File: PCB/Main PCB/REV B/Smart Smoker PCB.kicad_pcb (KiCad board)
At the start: 4 copper layers, 90 x 45 mm, 80 parts, among them J1 105017-0001, J2 393570002, J3 393570002, J4 393570002, J5 393570002, J6 393570002, J7 393570002, J8 Hopper, J9 Lid, Q1 Q_PMOS_GSD, Q2 25V 1.5A Trans, Q3 25V 1.5A Trans, Q4 Q_PMOS_GSD, Q5 2N7002T-7-F, Q6 2N7002T-7-F, U1 ESP32-WROOM-32UE_16MB, U2 DG409LEDY-T1-GE3, U3 MAX31855KASA, U4 AMS1117-3.3, U5 CP2102N-Axx-xQFN28, U6 LTC4412xS6

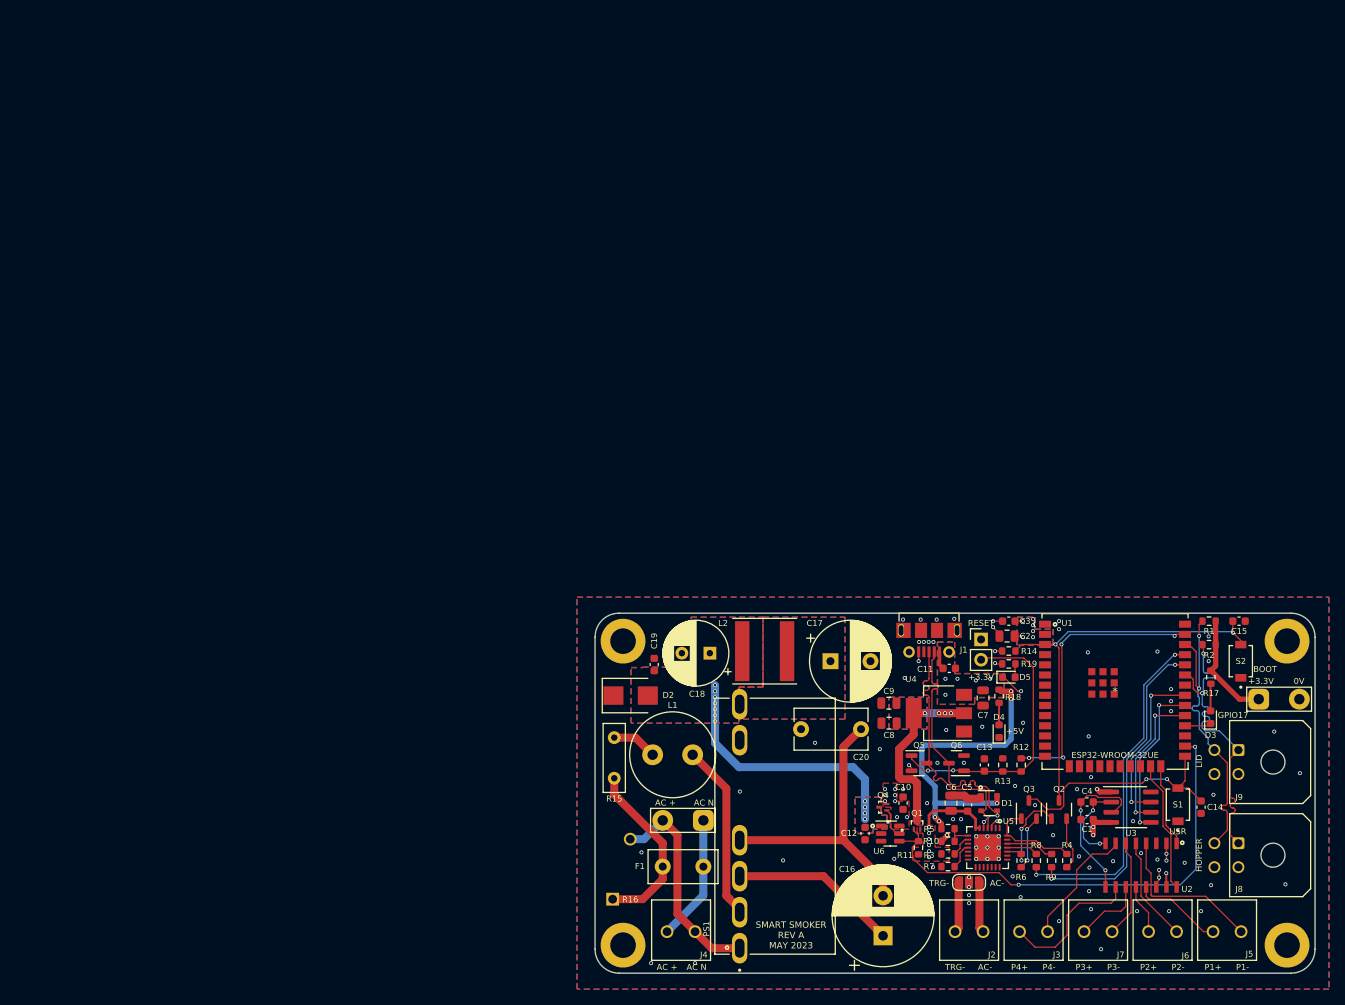
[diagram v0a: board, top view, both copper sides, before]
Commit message: Hardware Rev B development Relays and Rotary Encoder
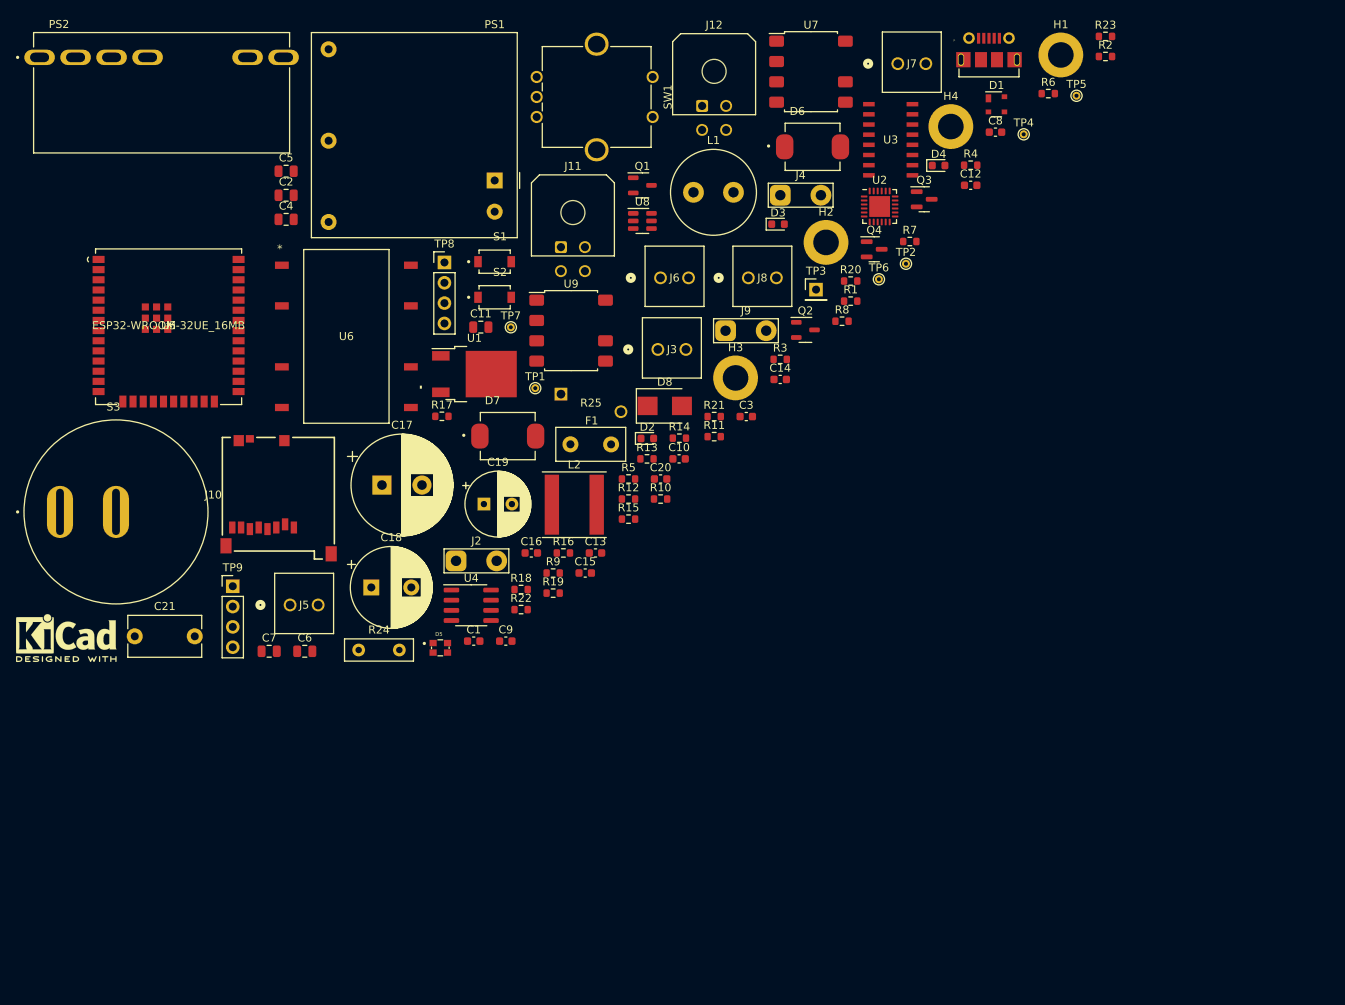
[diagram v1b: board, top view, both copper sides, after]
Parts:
- removed JP1: Jumper_2_Open, Connector_PinHeader_2.54mm:PinHeader_1x02_P2.54mm_Vertical
- removed JP2: Jumper_3_Open, Jumper:SolderJumper-3_P1.3mm_Open_RoundedPad1.0x1.5mm
- removed Q5, Q6: 2N7002T-7-F, Package_TO_SOT_SMD:SOT-23
- added C21: 1000pF 440VAC Y5P, Capacitor_THT:C_Disc_D9.0mm_W5.0mm_P7.50mm, F.Cu at (42.5, 102.9)
- added D6: D_TVS, Customs Smoker:DIOM7959X262N, F.Cu at (127.2, 41.7)
- added D7: D_TVS, Customs Smoker:DIOM7959X262N, F.Cu at (89.1, 77.9)
- added D8: TVS DIODE 7VWM 12VC SMB, Diode_SMD:D_SMB, F.Cu at (108.7, 74.1)
- added J10: MEM2051-00-195-00-A, Customs Smoker:GCT_MEM2051-00-195-00-A, F.Cu at (60.4, 85.6)
- added J11: Hopper, Connector_Molex:Molex_Micro-Fit_3.0_43045-0400_2x02_P3.00mm_Horizontal, F.Cu at (95.7, 54.2)
- added J12: Lid, Connector_Molex:Molex_Micro-Fit_3.0_43045-0400_2x02_P3.00mm_Horizontal, F.Cu at (113.4, 36.6)
- added PS2: LS10-13B03R3, Customs Smoker:CONV_LS10-13B03R3, F.Cu at (45.8, 30.5)
- added R20: 80.6Ohm 1% 0603, Resistor_SMD:R_0603_1608Metric, F.Cu at (132.0, 58.5)
- added R21: 470Ohm 5% 0603, Resistor_SMD:R_0603_1608Metric, F.Cu at (114.9, 75.4)
- added R22: 140Ohm 1% 0603, Resistor_SMD:R_0603_1608Metric, F.Cu at (90.8, 99.6)
- added R23: 80.6Ohm 1% 0603, Resistor_SMD:R_0603_1608Metric, F.Cu at (163.8, 27.9)
- added R24: 6.8Ohm 3W 5% 2512, Resistor_THT:R_Box_L8.4mm_W2.5mm_P5.08mm, F.Cu at (70.5, 104.6)
- added R25: B72214S0351K101, Customs Smoker:VARS_B72214S_15P5X5P6-7P5-2P2_TDK, F.Cu at (99.5, 73.7)
- added S3: RR511D1121, Customs Smoker:E-SWITCH_RR511D1121, F.Cu at (40.1, 87.3)
- added SW1: SW_Coded_SH-7050, Rotary_Encoder:RotaryEncoder_Bourns_Vertical_PEC12R-3xxxF-Sxxxx, F.Cu at (92.7, 33.0)
- added TP3: GND TP PIN, Connector_PinHeader_2.54mm:PinHeader_1x01_P2.54mm_Vertical, F.Cu at (127.6, 59.6)
- added TP4: 3V3 TP, TestPoint:TestPoint_THTPad_D1.0mm_Drill0.5mm, F.Cu at (153.6, 40.1)
- added TP5: 3V3 TP, TestPoint:TestPoint_THTPad_D1.0mm_Drill0.5mm, F.Cu at (160.2, 35.3)
- added TP6: SCL TP, TestPoint:TestPoint_THTPad_D1.0mm_Drill0.5mm, F.Cu at (135.5, 58.3)
- added TP7: SDA TP, TestPoint:TestPoint_THTPad_D1.0mm_Drill0.5mm, F.Cu at (89.5, 64.3)
- added TP8: GPIO MISC., Connector_PinHeader_2.54mm:PinHeader_1x04_P2.54mm_Vertical, F.Cu at (81.2, 56.2)
- added TP9: Screen I2C, Connector_PinHeader_2.54mm:PinHeader_1x04_P2.54mm_Vertical, F.Cu at (54.7, 96.6)
- added U7: AQH2223A, Package_SO:SSO-7-8_6.4x9.78mm_P2.54mm, F.Cu at (127.0, 32.3)
- added U8: LTC4412xS6, Package_TO_SOT_SMD:TSOT-23-6, F.Cu at (105.9, 51.0)
- added U9: AQH2223A, Package_SO:SSO-7-8_6.4x9.78mm_P2.54mm, F.Cu at (97.0, 64.7)
- AE1: moved to F.Cu
- C10: value 1uF 25V X5R 0603 -> 0.01uF 50V X7R 0603
- C11: value 0.1uF 50V X7R 0603 -> 22uF 10V X5R 0805; footprint Capacitor_SMD:C_0603_1608Metric -> Capacitor_SMD:C_0805_2012Metric
- C15: value 0.1uF 50V X7R 0603 -> 1uF 25V X5R 0603
- C16: value 22uF 450V 20% -> 0.1uF 50V X7R 0603; footprint Capacitor_THT:CP_Radial_D12.5mm_P5.00mm -> Capacitor_SMD:C_0603_1608Metric
- C17: value 820uF 20% 16V -> 22uF 450V 20%; footprint Capacitor_THT:CP_Radial_D10.0mm_P5.00mm -> Capacitor_THT:CP_Radial_D12.5mm_P5.00mm
- C18: value 150uF 20% 35V -> 820uF 20% 16V; footprint Capacitor_THT:CP_Radial_D8.0mm_P3.50mm -> Capacitor_THT:CP_Radial_D10.0mm_P5.00mm
- C19: value 0.1uF 50V X7R 0603 -> 150uF 20% 35V; footprint Capacitor_SMD:C_0603_1608Metric -> Capacitor_THT:CP_Radial_D8.0mm_P3.50mm
- C2: value 22uF 10V X5R 0805 -> 4.7uF 25V X5R 0805
- C20: value 1000pF 440VAC Y5P -> 0.1uF 50V X7R 0603; footprint Capacitor_THT:C_Disc_D9.0mm_W5.0mm_P7.50mm -> Capacitor_SMD:C_0603_1608Metric
- C4: value 0.01uF 50V X7R 0603 -> 10uF 16V X5R 0805; footprint Capacitor_SMD:C_0603_1608Metric -> Capacitor_SMD:C_0805_2012Metric
- C5: value 0.1uF 50V X7R 0603 -> 10uF 16V X5R 0805; footprint Capacitor_SMD:C_0603_1608Metric -> Capacitor_SMD:C_0805_2012Metric
- C6: value 4.7uF 25V X5R 0805 -> 10uF 16V X5R 0805
- C8, C9: value 10uF 16V X5R 0805 -> 0.1uF 50V X7R 0603; footprint Capacitor_SMD:C_0805_2012Metric -> Capacitor_SMD:C_0603_1608Metric
- D2: value TVS DIODE 7VWM 12VC SMB -> Y 2V 20mA; footprint Diode_SMD:D_SMB -> LED_SMD:LED_0603_1608Metric
- D3: value Y 2V 20mA -> Y/G 2.2V 20mA
- D4: value Y/G 2.2V 20mA -> R 1.8V 2mA 0603
- D5: value R 1.8V 2mA 0603 -> ASMB-KTF0-0A306; footprint LED_SMD:LED_0603_1608Metric -> Customs Smoker:LED_ASMB-KTF0-0A306
- J2: value 393570002 -> HEATER; footprint Customs Smoker:CONN_393570002_MOL -> TestPoint:TestPoint_2Pads_Pitch5.08mm_Drill1.3mm
- J4: value 393570002 -> AUGER; footprint Customs Smoker:CONN_393570002_MOL -> TestPoint:TestPoint_2Pads_Pitch5.08mm_Drill1.3mm
- J8: value Hopper -> 393570002; footprint Connector_Molex:Molex_Micro-Fit_3.0_43045-0400_2x02_P3.00mm_Horizontal -> Customs Smoker:CONN_393570002_MOL
- J9: value Lid -> FAN; footprint Connector_Molex:Molex_Micro-Fit_3.0_43045-0400_2x02_P3.00mm_Horizontal -> TestPoint:TestPoint_2Pads_Pitch5.08mm_Drill1.3mm
- PS1: value LS10-13B03R3 -> RAC05-3.3SK; footprint Customs Smoker:CONV_LS10-13B03R3 -> Converter_ACDC:Converter_ACDC_RECOM_RAC05-xxSK_THT
- Q1: value Q_PMOS_GSD -> 25V 1.5A Trans; footprint Customs Smoker:VESM_TOS -> Package_TO_SOT_SMD:SOT-23-3
- Q3: value 25V 1.5A Trans -> Q_PMOS_GSD; footprint Package_TO_SOT_SMD:SOT-23-3 -> Package_TO_SOT_SMD:SOT-23
- Q4: footprint Customs Smoker:VESM_TOS -> Package_TO_SOT_SMD:SOT-23
- R1: value 1.8kOhm 1% 0603 -> 1kOhm 1% 0603
- R10: value 47.5kOhm 1% 0603 -> 10K 1% 0603
- R11: value 470Ohm 5% 0603 -> 470Ohm 1% 0603
- R12: value 1kOhm 1% 0603 -> 140Ohm 1% 0603
- R13: value 10K 1% 0603 -> 140Ohm 1% 0603
- R14: value 10K 1% 0603 -> 750Ohm 1% 0603
- R15: value 6.8Ohm 3W 5% 2512 -> 80.6Ohm 1% 0603; footprint Resistor_THT:R_Box_L8.4mm_W2.5mm_P5.08mm -> Resistor_SMD:R_0603_1608Metric
- R16: value B72214S0351K101 -> 20Ohm 1% 0603; footprint Customs Smoker:VARS_B72214S_15P5X5P6-7P5-2P2_TDK -> Resistor_SMD:R_0603_1608Metric
- R17: value 470Ohm 1% 0603 -> 20Ohm 1% 0603
- R18: value 140Ohm 1% 0603 -> 64.9Ohm 1% 0603
- R19: value 750Ohm 1% 0603 -> 140Ohm 1% 0603
- R2: value 1.8kOhm 1% 0603 -> 10K 1% 0603
- R3: value 1kOhm 1% 0603 -> 22.1kOhm 1% 0603
- R5: value 22.1kOhm 1% 0603 -> 47.5kOhm 1% 0603
- R6, R7: value 10K 1% 0603 -> 0Ohm 0603
- R8, R9: value 0Ohm 0603 -> 1.8kOhm 1% 0603
- TP1: value TestPoint_2Pole -> 3V3 TP; footprint TestPoint:TestPoint_2Pads_Pitch5.08mm_Drill1.3mm -> TestPoint:TestPoint_THTPad_D1.0mm_Drill0.5mm
- TP2: value TestPoint_2Pole -> GND TP; footprint TestPoint:TestPoint_2Pads_Pitch5.08mm_Drill1.3mm -> TestPoint:TestPoint_THTPad_D1.0mm_Drill0.5mm
- U1: value ESP32-WROOM-32UE_16MB -> AMS1117-3.3; footprint Customs Smoker:ESP32-WROOM-32UE 16MB -> Package_TO_SOT_SMD:TO-252-2
- U2: value DG409LEDY-T1-GE3 -> CP2102N-Axx-xQFN20; footprint Customs Smoker:SOIC16_NARROW_VIS -> Package_DFN_QFN:QFN-24-1EP_4x4mm_P0.5mm_EP2.6x2.6mm
- U3: value MAX31855KASA -> DG409LEDY-T1-GE3; footprint Package_SO:SOIC-8_3.9x4.9mm_P1.27mm -> Customs Smoker:SOIC16_NARROW_VIS
- U4: value AMS1117-3.3 -> MAX31855KASA; footprint Package_TO_SOT_SMD:SOT-223-3_TabPin2 -> Package_SO:SOIC-8_3.9x4.9mm_P1.27mm
- U5: value CP2102N-Axx-xQFN28 -> ESP32-WROOM-32UE_16MB; footprint Package_DFN_QFN:QFN-28-1EP_5x5mm_P0.5mm_EP3.35x3.35mm -> Customs Smoker:ESP32-WROOM-32UE 16MB
- U6: value LTC4412xS6 -> CPC1966B; footprint Package_TO_SOT_SMD:TSOT-23-6 -> Customs Smoker:CPC1966B_IXY
- moved C4 123.8 mm to (61.4, 50.8)
- moved J5 122.4 mm to (61.9, 99.0)
- moved U5 121.3 mm to (46.7, 64.2), turned to 0 degrees
- moved C5 116.3 mm to (61.4, 44.8), turned to 0 degrees
- moved J7 111.0 mm to (137.8, 31.3)
- moved H4 110.2 mm to (144.5, 39.2)
- moved S1 109.1 mm to (87.4, 56.1), turned to 0 degrees
- moved C2 105.6 mm to (61.4, 47.8)
- moved H2 105.1 mm to (128.9, 53.7)
- moved S2 103.8 mm to (87.4, 60.5), turned to 0 degrees
- moved J6 102.0 mm to (108.2, 58.1)
- moved R17 101.5 mm to (80.9, 75.4), turned to 0 degrees
- moved R6 95.9 mm to (156.7, 35.1), turned to 0 degrees
- moved J8 93.5 mm to (119.2, 58.1), turned to 0 degrees
- moved J4 93.1 mm to (123.2, 47.8)
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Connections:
- C1 pad 1: +3.3V -> GND
- C1 pad 2: GND -> +3.3V
- C10 pad 1: GND -> /MUX_OUT_+
- C10 pad 2: +3.3V -> /MUX_OUT_-
- C11 pad 1: +5V -> GND
- C11 pad 2: GND -> +3.3V
- C12 pad 1: +3.3VA -> GND
- C12 pad 2: GND -> +3.3V
- C13 pad 1: GND -> /EN
- C13 pad 2: Net-(C13-Pad2) -> GND
- C14 pad 1: GND -> /IO0
- C14 pad 2: /IO0 -> GND
- C15 pad 1: /EN -> GND
- C15 pad 2: GND -> +3.3V
- C16 pad 1: Net-(C16-Pad1) -> +3.3VA
- C16 pad 2: Net-(C16-Pad2) -> GND
- C17 pad 2: GND -> Net-(C17-Pad2)
- C18 pad 1: +3.3VA -> Net-(C18-Pad1)
- C20 pad 1: Net-(C16-Pad2) -> +3.3VA
- C3 pad 1: GND -> Net-(C3-Pad1)
- C3 pad 2: +3.3V -> Net-(C3-Pad2)
- C4 pad 1: /MUX_OUT_+ -> Net-(C3-Pad2)
- C4 pad 2: /MUX_OUT_- -> Net-(C3-Pad1)
- C5 pad 1: GND -> +5V
- C5 pad 2: +3.3V -> GND
- C6 pad 1: GND -> +3.3VP
- C6 pad 2: +3.3V -> GND
- C7 pad 1: +5V -> +3.3VP
- C8 pad 1: +3.3VP -> +3.3V
- C9 pad 1: +3.3VP -> +5V
- D2 pad 1: GND -> /IO17
- D2 pad 2: +3.3VA -> Net-(D2-Pad2)
- D3 pad 1: /IO17 -> GND
- D5 pad 1: GND -> +3.3V
- J2 pad 1: /TRG_GND -> /Heater_+
- J2 pad 2: /AC_G -> /AC_N
- J4 pad 1: /AC_L -> /Auger_+
- J5 pad 1: /Probe1+ -> /AC_L
- J5 pad 2: /Probe1- -> /AC_N
- J6 pad 1: /Probe2+ -> /Probe1+
- J6 pad 2: /Probe2- -> /Probe1-
- J7 pad 1: /Probe3+ -> /Probe2+
- J7 pad 2: /Probe3- -> /Probe2-
- J8 pad 1: /I2C_SDA -> /Probe3+
- J8 pad 2: GND -> /Probe3-
- J9 pad 1: /I2C_SDA -> /Fan_+
- J9 pad 2: GND -> /AC_N
- L2 pad 1: Net-(C17-Pad1) -> Net-(C18-Pad1)
- PS1 pad 1: /AC_N -> unconnected-(PS1-Pad1)
- PS1 pad 2: Net-(L1-Pad2) -> unconnected-(PS1-Pad2)
- PS1 pad 3: Net-(C16-Pad1) -> unconnected-(PS1-Pad3)
- PS1 pad 4: Net-(C16-Pad2) -> Net-(C3-Pad1)
- PS1 pad 5: GND -> Net-(C3-Pad2)
- Q1 pad 1: /IO4 -> /RTS
- Q1 pad 2: +3.3V -> Net-(Q1-Pad2)
- Q1 pad 3: +3.3VP -> /EN
- Q2 pad 1: /RTS -> /DTR
- Q2 pad 3: /EN -> /IO0
- Q3 pad 1: /DTR -> /IO4
- Q3 pad 2: Net-(Q3-Pad2) -> +3.3V
- Q3 pad 3: /IO0 -> +3.3VP
- Q4 pad 1: Net-(Q4-Pad1) -> Net-(U8-Pad5)
- R1 pad 1: /I2C_SCL -> Net-(R1-Pad1)
- R10 pad 1: GND -> /EN
- R10 pad 2: Net-(R10-Pad2) -> +3.3V
- R11 pad 1: /IO4 -> +3.3V
- R11 pad 2: +3.3V -> Net-(D2-Pad2)
- R12 pad 1: /IO23 -> +5V
- R12 pad 2: Net-(C13-Pad2) -> Net-(D3-Pad2)
- R13 pad 1: Net-(C13-Pad2) -> unconnected-(R13-Pad1)
- R13 pad 2: GND -> Net-(R13-Pad2)
- R14 pad 1: /EN -> +3.3V
- R14 pad 2: +3.3V -> Net-(D4-Pad2)
- R15 pad 1: Net-(F1-Pad2) -> Net-(R13-Pad2)
- R15 pad 2: Net-(L1-Pad1) -> GND
- R16 pad 1: Net-(F1-Pad2) -> Net-(D5-Pad3)
- R16 pad 2: /AC_N -> /IO26
- R17 pad 1: +3.3V -> Net-(D5-Pad4)
- R17 pad 2: Net-(D3-Pad2) -> /IO27
- R18 pad 1: +5V -> Net-(D5-Pad2)
- R18 pad 2: Net-(D4-Pad2) -> /IO25
- R19 pad 1: +3.3V -> unconnected-(R19-Pad1)
- R19 pad 2: Net-(D5-Pad2) -> Net-(R19-Pad2)
- R2 pad 1: /I2C_SDA -> /DTR
- R2 pad 2: +3.3V -> Net-(Q1-Pad2)
- R3 pad 1: Net-(R3-Pad1) -> +5V
- R3 pad 2: +3.3V -> Net-(R3-Pad2)
- R4 pad 1: /DTR -> /RTS
- R5 pad 1: +5V -> GND
- R5 pad 2: Net-(R10-Pad2) -> Net-(R3-Pad2)
- R6 pad 1: /RTS -> /TXD0
- R6 pad 2: Net-(Q3-Pad2) -> /RXD
- R7 pad 1: GND -> /RXD0
- R7 pad 2: Net-(R7-Pad2) -> /TXD
- R8 pad 1: /TXD0 -> /I2C_SCL
- R8 pad 2: /RXD -> +3.3V
- R9 pad 1: /RXD0 -> /I2C_SDA
- R9 pad 2: /TXD -> +3.3V
- S1 pad 2: /IO0 -> /EN
- S2 pad 2: /EN -> /IO0
- TP1 pad 1: /AC_L -> +3.3V
- TP2 pad 1: +3.3V -> GND
- U1 pad 2: +3.3V -> +3.3VP
- U1 pad 3: /EN -> +5V
- U2 pad 1: /IO2 -> unconnected-(U2-Pad1)
- U2 pad 10: /Probe4+ -> unconnected-(U2-Pad10)
- U2 pad 11: /Probe3+ -> unconnected-(U2-Pad11)
- U2 pad 12: /Probe2+ -> unconnected-(U2-Pad12)
- U2 pad 13: /Probe1+ -> unconnected-(U2-Pad13)
- U2 pad 14: +3.3V -> unconnected-(U2-Pad14)
- U2 pad 15: GND -> unconnected-(U2-Pad15)
- U2 pad 16: /IO15 -> unconnected-(U2-Pad16)
- U2 pad 2: +3.3V -> GND
- U2 pad 3: GND -> /USB_DP
- U2 pad 4: /Probe1- -> /USB_DN
- U2 pad 5: /Probe2- -> +3.3V
- U2 pad 6: /Probe3- -> +3.3V
- U2 pad 7: /Probe4- -> +3.3V
- U2 pad 8: /MUX_OUT_- -> Net-(R3-Pad2)
- U2 pad 9: /MUX_OUT_+ -> Net-(R1-Pad1)
- U3 pad 1: GND -> /IO2
- U3 pad 2: /MUX_OUT_- -> +3.3V
- U3 pad 3: /MUX_OUT_+ -> GND
- U3 pad 4: +3.3V -> /Probe1-
- U3 pad 5: /SPI_SCK -> /Probe2-
- U3 pad 6: /SPI_CS -> /Probe3-
- U3 pad 7: /SPI_MISO -> /Probe4-
- U3 pad 8: (no net) -> /MUX_OUT_-
- U4 pad 2: +3.3VP -> /MUX_OUT_-
- U4 pad 3: +5V -> /MUX_OUT_+
- U5 pad 1: unconnected-(U5-Pad1) -> GND
- U5 pad 10: unconnected-(U5-Pad10) -> /IO25
- U5 pad 11: Net-(R7-Pad2) -> /IO26
- U5 pad 12: unconnected-(U5-Pad12) -> /IO27
- U5 pad 13: unconnected-(U5-Pad13) -> /IO14
- U5 pad 14: unconnected-(U5-Pad14) -> /IO12
- U5 pad 15: unconnected-(U5-Pad15) -> GND
- U5 pad 16: unconnected-(U5-Pad16) -> /IO13
- U5 pad 2: unconnected-(U5-Pad2) -> +3.3V
- U5 pad 23: /CTS -> /IO15
- U5 pad 24: /RTS -> /IO2
- U5 pad 25: /RXD -> /IO0
- U5 pad 26: /TXD -> /IO4
- U5 pad 27: unconnected-(U5-Pad27) -> /IO16
- U5 pad 28: /DTR -> /IO17
- U5 pad 29: GND -> /SPI_CS
- U5 pad 3: GND -> /EN
- U5 pad 4: /USB_DP -> /I36
- U5 pad 5: /USB_DN -> /I39
- U5 pad 6: +3.3V -> /I34
- U5 pad 7: +3.3V -> /I35
- U5 pad 8: Net-(R10-Pad2) -> /IO32
- U5 pad 9: Net-(R3-Pad1) -> /IO33
- U6 pad 1: +3.3VA -> unconnected-(U6-Pad1)
- U6 pad 2: GND -> Net-(R13-Pad2)
- U6 pad 4: /IO4 -> unconnected-(U6-Pad4)
- U6 pad 5: Net-(Q4-Pad1) -> /AC_L
- U6 pad 6: +3.3V -> /AC_L
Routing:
- net /IO4: track 60.5 -> 0.00 mm, vias 2 -> 0
- net /EN: track 51.3 -> 0.00 mm, vias 2 -> 0
- net +5V: track 42.9 -> 0.00 mm, vias 10 -> 0
- net /TXD0: track 42.7 -> 0.00 mm, vias 2 -> 0
- net /RXD0: track 41.0 -> 0.00 mm, vias 2 -> 0
- net /I2C_SCL: track 38.4 -> 0.00 mm, vias 2 -> 0
- net /I2C_SDA: track 38.1 -> 0.00 mm, vias 2 -> 0
- net Net-(C16-Pad2): track 36.8 -> 0.00 mm
- net /IO23: track 35.7 -> 0.00 mm, vias 4 -> 0
- net +3.3V: track 35.6 -> 0.00 mm, vias 28 -> 0
- net Net-(C13-Pad2): track 35.0 -> 0.00 mm, vias 2 -> 0
- net +3.3VA: track 32.9 -> 0.00 mm, vias 11 -> 0
- net /USB_DN: track 32.2 -> 0.00 mm, vias 2 -> 0
- net /USB_DP: track 31.4 -> 0.00 mm
- net /IO0: track 29.9 -> 0.00 mm, vias 2 -> 0
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- removed copper zone on B.Cu, net +3.3V
- removed copper zone on F.Cu, net +3.3V
- removed copper zone on In2.Cu, net +3.3V
- removed copper zone on B.Cu, net +3.3VA
- removed copper zone on F.Cu, net +3.3VA
- removed copper zone on B.Cu, net +3.3VP
- removed copper zone on F.Cu, net +3.3VP
- removed copper zone on B.Cu, net +5V
- removed copper zone on F.Cu, net +5V
- removed copper zone on B.Cu, net GND
- removed copper zone on F.Cu, net GND
- removed copper zone on In1.Cu, net GND
- removed copper zone on B.Cu, net Net-(C17-Pad1)
- removed copper zone on F.Cu, net Net-(C17-Pad1)
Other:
- board outline removed
- board text removed: "+3.3V"
- board text removed: "+5V"
- board text removed: "0V"
- board text removed: "90 x 45mm H M3x83x38mm"
- board text removed: "AC +"
- board text removed: "AC N"
- board text removed: "AC-"
- board text removed: "BOOT"
- board text removed: "ESP32-WROOM-32UE"
- board text removed: "GPIO17"
- board text removed: "HOPPER"
- board text removed: "LID"
- board text removed: "P1+"
- board text removed: "P1-"
- board text removed: "P2+"
- board text removed: "P2-"
- board text removed: "P3+"
- board text removed: "P3-"
- board text removed: "P4+"
- board text removed: "P4-"
- board text removed: "RESET"
- board text removed: "SMART SMOKER REV A MAY 2023"
- board text removed: "Smart Smoker PCB REV A May 2023"
- board text removed: "TRG-"
- board text removed: "USR"
